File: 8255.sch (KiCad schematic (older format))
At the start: 7 parts, among them U7 PAL16L8

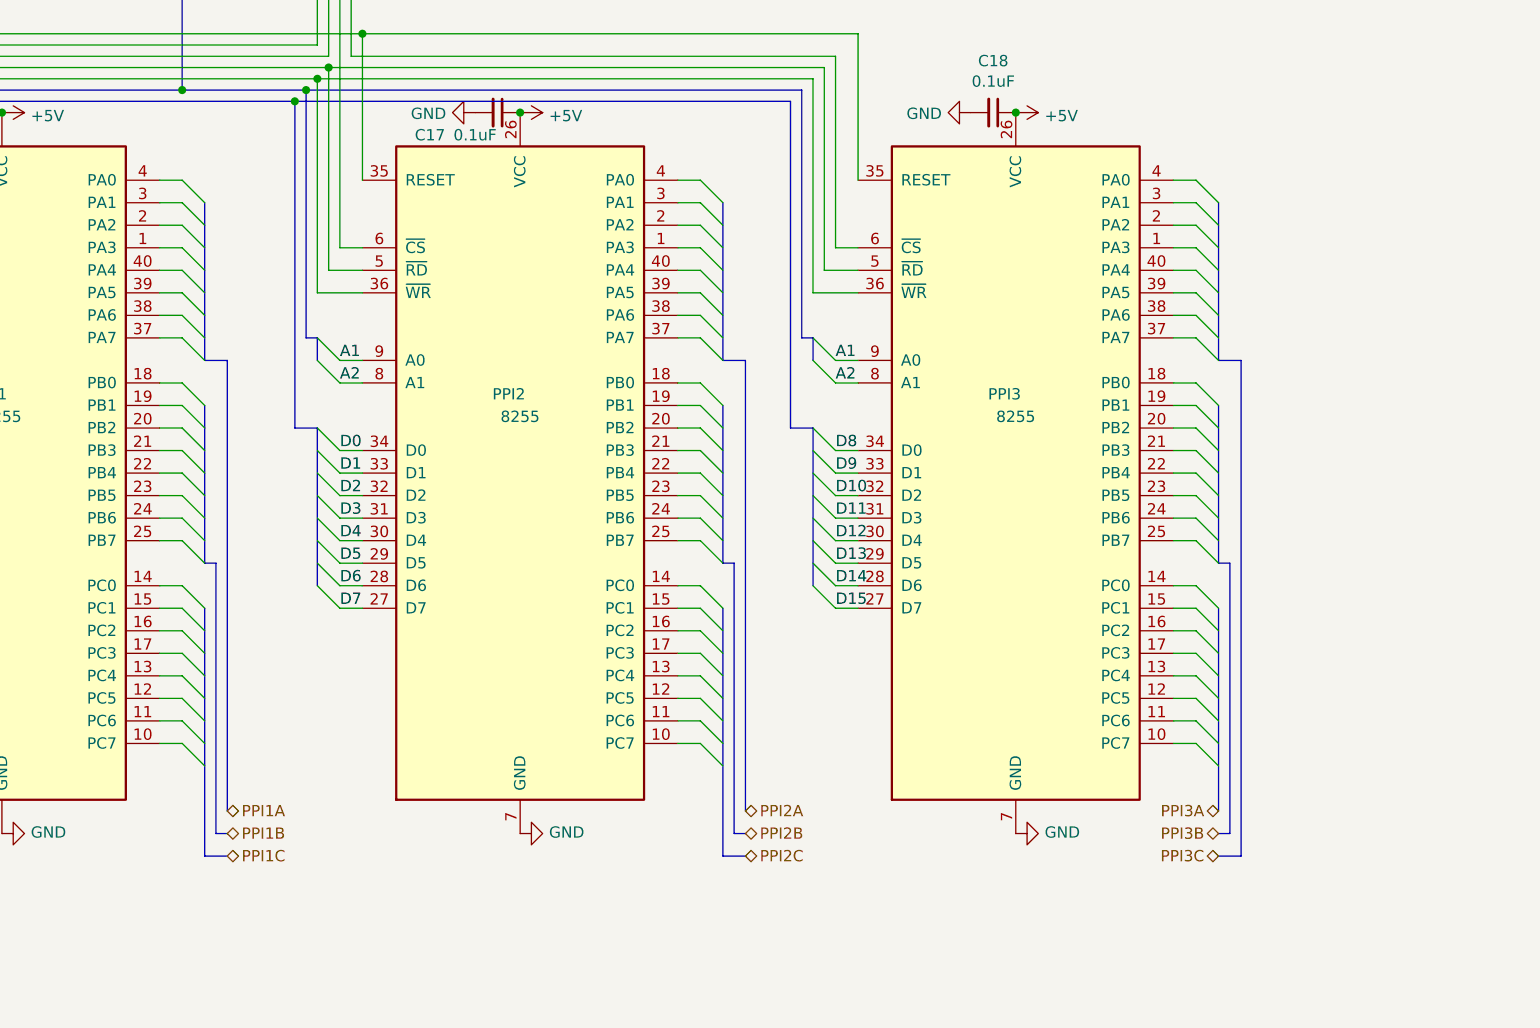
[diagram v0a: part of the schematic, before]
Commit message: Added external headers
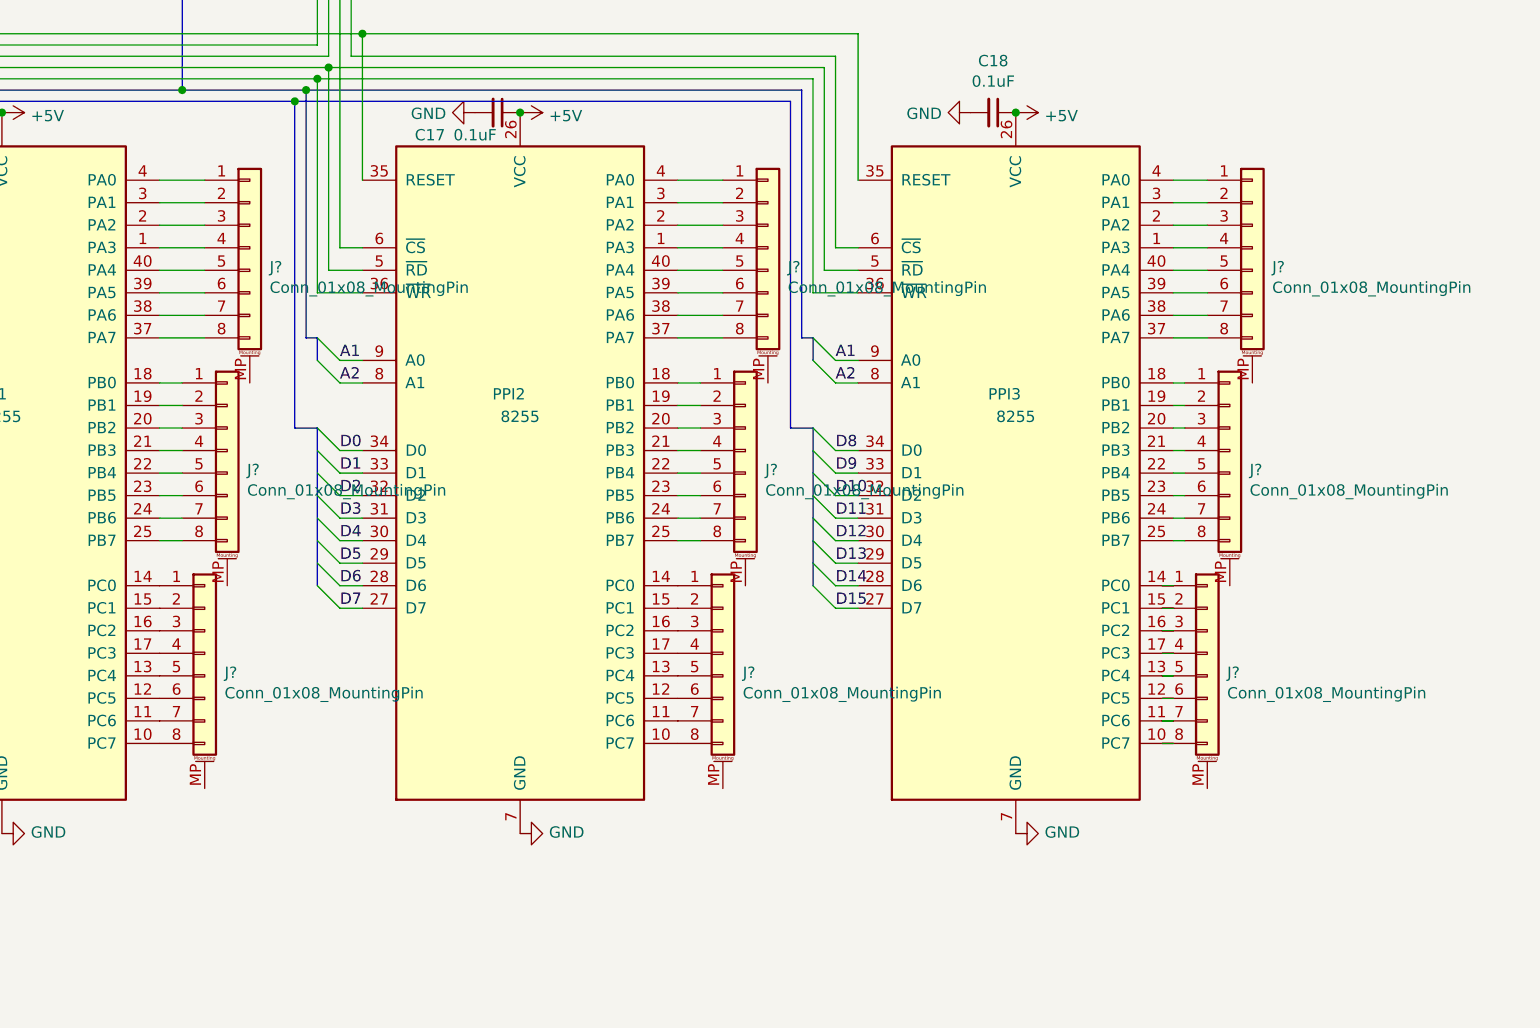
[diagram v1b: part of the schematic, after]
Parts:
- added J? (x9): Conn_01x08_MountingPin, symbol Connector_Generic_MountingPin:Conn_01x08_MountingPin
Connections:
- net at PPI1.1 (PA3): now also J?.4 (Pin_4)
- net at PPI1.10 (PC7): now also J?.8 (Pin_8)
- net at PPI1.11 (PC6): now also J?.7 (Pin_7)
- net at PPI1.12 (PC5): now also J?.6 (Pin_6)
- net at PPI1.13 (PC4): now also J?.5 (Pin_5)
- net at PPI1.14 (PC0): now also J?.1 (Pin_1)
- net at PPI1.15 (PC1): now also J?.2 (Pin_2)
- net at PPI1.16 (PC2): now also J?.3 (Pin_3)
- net at PPI1.17 (PC3): now also J?.4 (Pin_4)
- net at PPI1.18 (PB0): now also J?.1 (Pin_1)
- net at PPI1.19 (PB1): now also J?.2 (Pin_2)
- net at PPI1.2 (PA2): now also J?.3 (Pin_3)
- net at PPI1.20 (PB2): now also J?.3 (Pin_3)
- net at PPI1.21 (PB3): now also J?.4 (Pin_4)
- net at PPI1.22 (PB4): now also J?.5 (Pin_5)
- net at PPI1.23 (PB5): now also J?.6 (Pin_6)
- net at PPI1.24 (PB6): now also J?.7 (Pin_7)
- net at PPI1.25 (PB7): now also J?.8 (Pin_8)
- net at PPI1.3 (PA1): now also J?.2 (Pin_2)
- net at PPI1.37 (PA7): now also J?.8 (Pin_8)
- net at PPI1.38 (PA6): now also J?.7 (Pin_7)
- net at PPI1.39 (PA5): now also J?.6 (Pin_6)
- net at PPI1.4 (PA0): now also J?.1 (Pin_1)
- net at PPI1.40 (PA4): now also J?.5 (Pin_5)
- net at PPI2.1 (PA3): now also J?.4 (Pin_4)
- net at PPI2.10 (PC7): now also J?.8 (Pin_8)
- net at PPI2.11 (PC6): now also J?.7 (Pin_7)
- net at PPI2.12 (PC5): now also J?.6 (Pin_6)
- net at PPI2.13 (PC4): now also J?.5 (Pin_5)
- net at PPI2.14 (PC0): now also J?.1 (Pin_1)
- net at PPI2.15 (PC1): now also J?.2 (Pin_2)
- net at PPI2.16 (PC2): now also J?.3 (Pin_3)
- net at PPI2.17 (PC3): now also J?.4 (Pin_4)
- net at PPI2.18 (PB0): now also J?.1 (Pin_1)
- net at PPI2.19 (PB1): now also J?.2 (Pin_2)
- net at PPI2.2 (PA2): now also J?.3 (Pin_3)
- net at PPI2.20 (PB2): now also J?.3 (Pin_3)
- net at PPI2.21 (PB3): now also J?.4 (Pin_4)
- net at PPI2.22 (PB4): now also J?.5 (Pin_5)
- net at PPI2.23 (PB5): now also J?.6 (Pin_6)
- net at PPI2.24 (PB6): now also J?.7 (Pin_7)
- net at PPI2.25 (PB7): now also J?.8 (Pin_8)
- net at PPI2.3 (PA1): now also J?.2 (Pin_2)
- net at PPI2.37 (PA7): now also J?.8 (Pin_8)
- net at PPI2.38 (PA6): now also J?.7 (Pin_7)
- net at PPI2.39 (PA5): now also J?.6 (Pin_6)
- net at PPI2.4 (PA0): now also J?.1 (Pin_1)
- net at PPI2.40 (PA4): now also J?.5 (Pin_5)
- net at PPI3.1 (PA3): now also J?.4 (Pin_4)
- net at PPI3.10 (PC7): now also J?.8 (Pin_8)
- net at PPI3.11 (PC6): now also J?.7 (Pin_7)
- net at PPI3.12 (PC5): now also J?.6 (Pin_6)
- net at PPI3.13 (PC4): now also J?.5 (Pin_5)
- net at PPI3.14 (PC0): now also J?.1 (Pin_1)
- net at PPI3.15 (PC1): now also J?.2 (Pin_2)
- net at PPI3.16 (PC2): now also J?.3 (Pin_3)
- net at PPI3.17 (PC3): now also J?.4 (Pin_4)
- net at PPI3.18 (PB0): now also J?.1 (Pin_1)
- net at PPI3.19 (PB1): now also J?.2 (Pin_2)
- net at PPI3.2 (PA2): now also J?.3 (Pin_3)
- net at PPI3.20 (PB2): now also J?.3 (Pin_3)
- net at PPI3.21 (PB3): now also J?.4 (Pin_4)
- net at PPI3.22 (PB4): now also J?.5 (Pin_5)
- net at PPI3.23 (PB5): now also J?.6 (Pin_6)
- net at PPI3.24 (PB6): now also J?.7 (Pin_7)
- net at PPI3.25 (PB7): now also J?.8 (Pin_8)
- net at PPI3.3 (PA1): now also J?.2 (Pin_2)
- net at PPI3.37 (PA7): now also J?.8 (Pin_8)
- net at PPI3.38 (PA6): now also J?.7 (Pin_7)
- net at PPI3.39 (PA5): now also J?.6 (Pin_6)
- net at PPI3.4 (PA0): now also J?.1 (Pin_1)
- net at PPI3.40 (PA4): now also J?.5 (Pin_5)

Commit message: Fixing Weirdness
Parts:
- removed J? (x9): Conn_01x08_MountingPin, symbol Connector_Generic_MountingPin:Conn_01x08_MountingPin
